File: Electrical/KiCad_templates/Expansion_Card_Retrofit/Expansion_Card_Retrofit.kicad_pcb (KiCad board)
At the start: 4 copper layers, 26 x 30 mm, 51 parts, among them J1 Conn 10P, P1 USB_C_Plug_USB2.0, Q1 DMG1012T, Q2 Q_PMOS_SGD, Q3 Q_Dual_NPN_NPN_C2E2C1E1B1B2, U1 AP2112K-3.3, U2 RP2040, U3 W25Q16JVUXIQ, U4 RP2040, U5 W25Q16JVUXIQ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

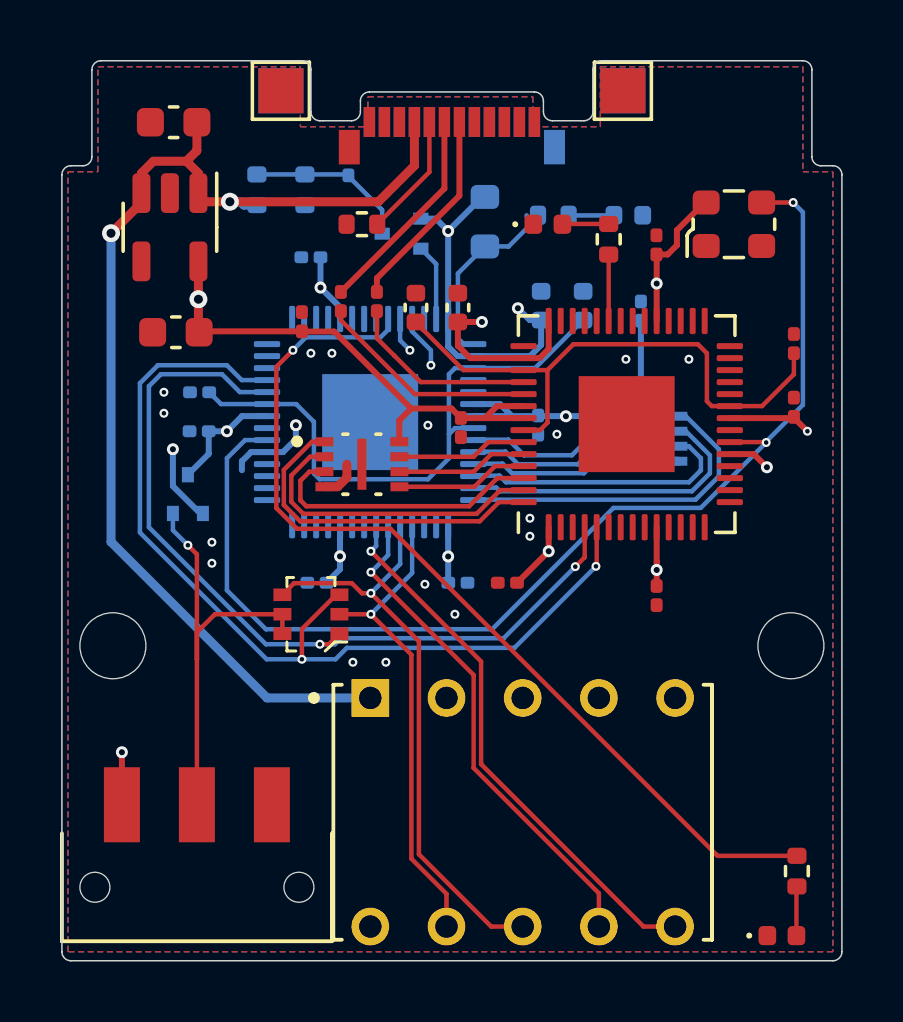
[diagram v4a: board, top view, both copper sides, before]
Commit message: All footprints placed single-sided
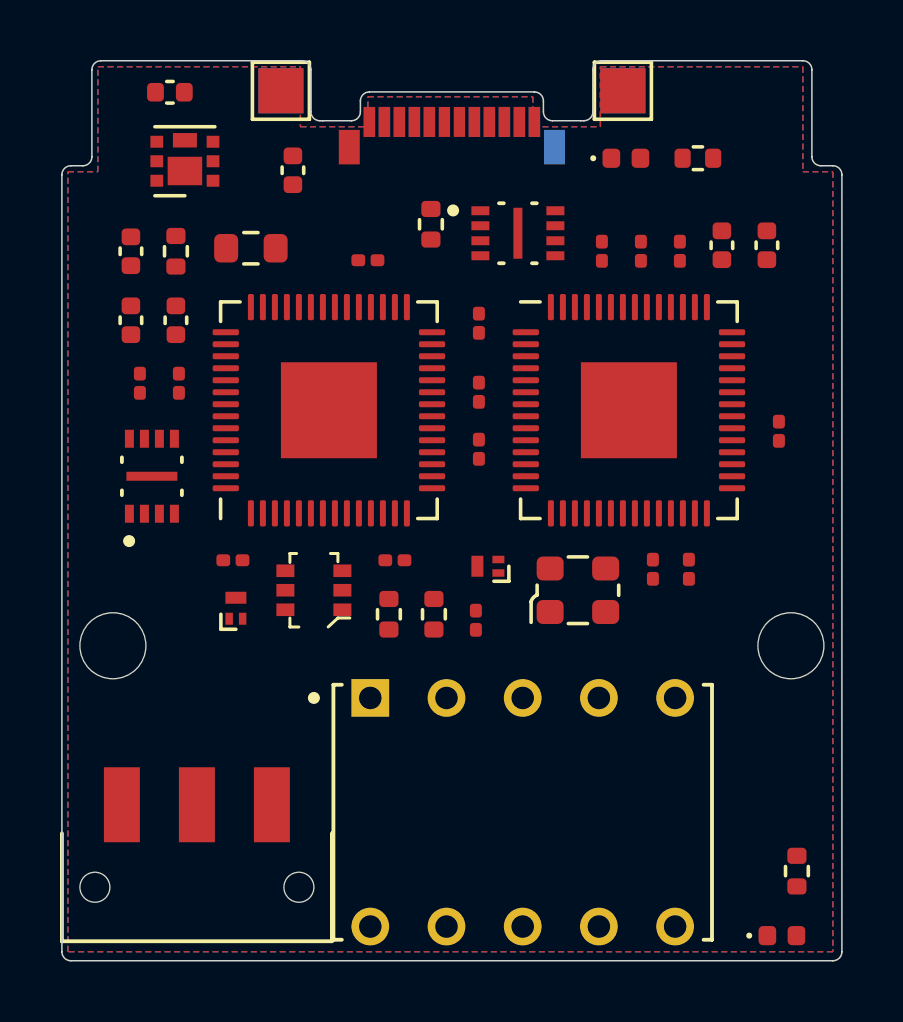
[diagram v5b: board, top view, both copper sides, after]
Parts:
- removed C17, C23: 100n, Capacitor_SMD:C_0201_0603Metric
- C1, C2: footprint Capacitor_SMD:C_0603_1608Metric -> Capacitor_SMD:C_0402_1005Metric
- C10, C11, C18, C22, C24, C5, C6, C7, C8, C9, R11, R12, R15, R16, U2, U3: moved to F.Cu
- Q1, Q2: footprint Package_TO_SOT_SMD:SOT-523 -> Package_DFN_QFN:Diodes_DFN1006-3; moved to F.Cu
- U1: value AP2112K-3.3 -> AP7366EA-3.3; footprint Package_TO_SOT_SMD:SOT-23-5 -> Package_DFN_QFN:Diodes_UDFN2020-6_Type-F
- moved C11 16.9 mm to (129.9, 95.8)
- moved C9 16.6 mm to (129.6, 91.4), turned to 90 degrees
- moved U3 16.3 mm to (130.3, 98.9), turned to 90 degrees
- moved C18 15.7 mm to (141.1, 103.7), turned to -90 degrees
- moved C7 15.1 mm to (129.6, 93.7)
- moved R15 14.8 mm to (138.2, 103.5)
- moved R16 14.8 mm to (139.7, 103.5)
- moved X1 13.3 mm to (144.5, 102.7)
- moved R12 12.6 mm to (131.1, 91.4), turned to -90 degrees
- moved C8 12.2 mm to (131.1, 93.7)
- moved C6 12.1 mm to (131.2, 95.8), turned to 90 degrees
- moved Q1 11.5 mm to (141.5, 101.9)
- moved C15 10.5 mm to (150.8, 91.2)
- moved C14 10.4 mm to (149.3, 91.2)
- moved R10 10.2 mm to (147.9, 91.4)
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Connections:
- C10 pad 1: /Development Board Section/3V3_DEV -> +3V3
- C11 pad 1: /Development Board Section/3V3_DEV -> +3V3
- C12 pad 1: +1V1 -> /Debug Probe Section/1V1_CORE
- C14 pad 1: +1V1 -> /Debug Probe Section/1V1_CORE
- C22 pad 1: /Development Board Section/3V3_DEV -> +3V3
- C24 pad 1: /Development Board Section/3V3_DEV -> +3V3
- C5 pad 1: +1V1 -> /Development Board Section/1V1_CORE
- C6 pad 1: /Development Board Section/3V3_DEV -> +3V3
- C7 pad 1: +1V1 -> /Development Board Section/1V1_CORE
- C8 pad 1: /Development Board Section/3V3_DEV -> +3V3
- Q1 pad 1: /Development Board Section/3V3_DEV -> +3V3
- Q2 pad 3: /Development Board Section/3V3_DEV -> /Development Board Section/RUN
- R11 pad 1: /Development Board Section/3V3_DEV -> +3V3
- U1 pad 4: unconnected-(U1-NC-Pad4) -> +3V3
- U1 pad 5: +3V3 -> unconnected-(U1-NC-Pad5)
- U2 pad 1: /Development Board Section/3V3_DEV -> +3V3
- U2 pad 10: /Development Board Section/3V3_DEV -> +3V3
- U2 pad 22: /Development Board Section/3V3_DEV -> +3V3
- U2 pad 23: +1V1 -> /Development Board Section/1V1_CORE
- U2 pad 26: unconnected-(U2-RUN-Pad26) -> /Development Board Section/RUN
- U2 pad 33: /Development Board Section/3V3_DEV -> +3V3
- U2 pad 42: /Development Board Section/3V3_DEV -> +3V3
- U2 pad 44: /Development Board Section/3V3_DEV -> +3V3
- U2 pad 45: +1V1 -> /Development Board Section/1V1_CORE
- U2 pad 48: /Development Board Section/3V3_DEV -> +3V3
- U2 pad 49: /Development Board Section/3V3_DEV -> +3V3
- U2 pad 50: +1V1 -> /Development Board Section/1V1_CORE
- U3 pad 8: /Development Board Section/3V3_DEV -> +3V3
- U4 pad 23: +1V1 -> /Debug Probe Section/1V1_CORE
- U4 pad 45: +1V1 -> /Debug Probe Section/1V1_CORE
- U4 pad 50: +1V1 -> /Debug Probe Section/1V1_CORE
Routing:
- net +3V3: track 39.7 -> 0.00 mm, vias 8 -> 0
- net +1V1: track 38.6 -> 0.00 mm
- net VBUS: track 38.2 -> 0.00 mm, vias 2 -> 0
- net OSC_OUT: track 38.0 -> 0.00 mm, vias 2 -> 0
- net SWDIO: track 31.9 -> 0.00 mm, vias 2 -> 0
- net LED_EN: track 31.5 -> 0.00 mm, vias 1 -> 0
- net /Development Board Section/3V3_DEV: track 31.4 -> 0.00 mm, vias 7 -> 0
- net SWCLK: track 28.2 -> 0.00 mm, vias 2 -> 0
- net GPIO3: track 19.7 -> 0.00 mm, vias 1 -> 0
- net GPIO5: track 18.3 -> 0.00 mm, vias 1 -> 0
- net GPIO4: track 16.8 -> 0.00 mm, vias 1 -> 0
- net GPIO_ADC0: track 16.4 -> 0.00 mm, vias 1 -> 0
- net GPIO2: track 16.0 -> 0.00 mm, vias 1 -> 0
- net DEV_ENABLE: track 14.7 -> 0.00 mm, vias 1 -> 0
- net GPIO_ADC1: track 14.3 -> 0.00 mm, vias 1 -> 0
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- added copper zone on In2.Cu, net +3V3
- removed copper zone on In2.Cu, net /Development Board Section/3V3_DEV

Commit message: Single layer basic layout finished
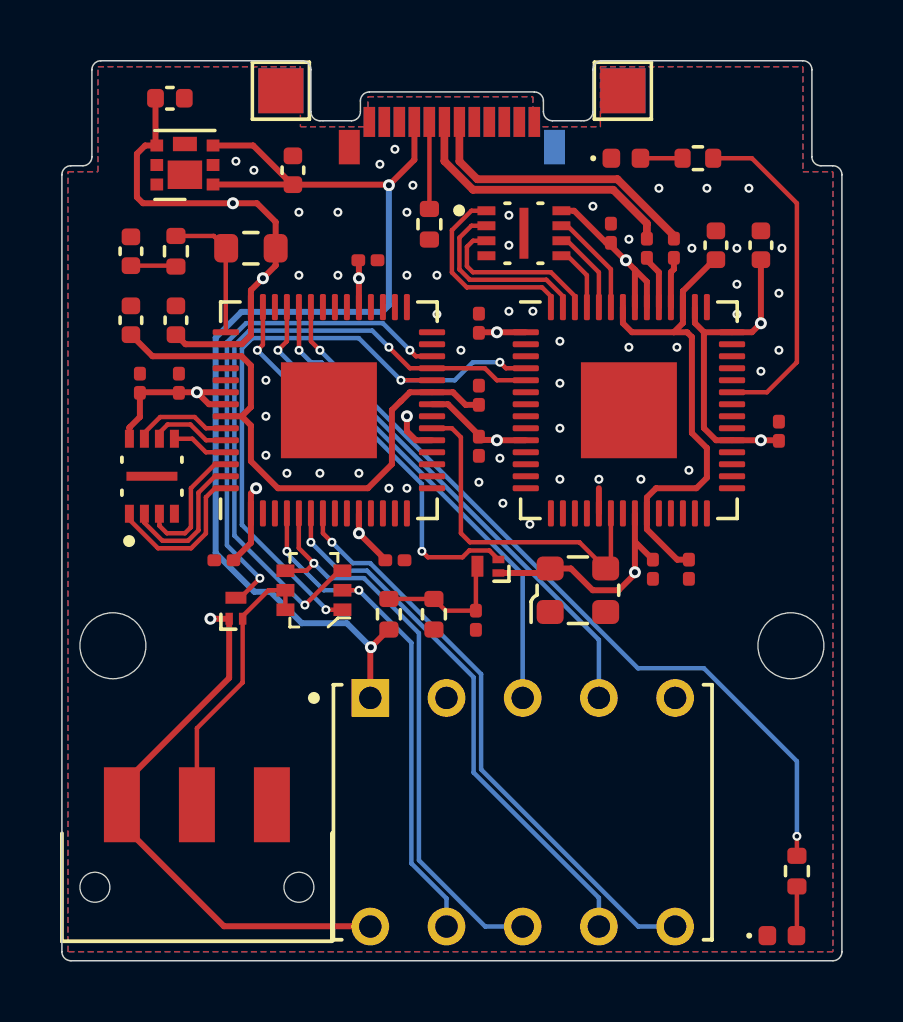
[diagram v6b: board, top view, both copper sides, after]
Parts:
- moved C13 0.67 mm to (145.6, 90.8)
- moved C10 0.30 mm to (132.7, 101.7)
- moved R10 0.22 mm to (147.7, 91.3)
- moved R9 0.22 mm to (146.8, 91.3)
- moved C14 0.20 mm to (149.1, 91.2)
- moved C15 0.20 mm to (150.6, 91.2)
- moved C2 0.20 mm to (130.9, 86.3)
- moved U5 0.20 mm to (142.7, 90.8)
- moved U1 0.12 mm to (131.4, 88.5)
- moved C5 0.10 mm to (141.2, 96.2), turned to 90 degrees
- moved C19 0.10 mm to (141.2, 97.9)
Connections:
- net USB_DN renamed USB_D_N
- net USB_DP renamed USB_D_P
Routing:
- net +3V3: track 0.00 -> 77.2 mm, vias 0 -> 13
- net VBUS: track 0.00 -> 38.0 mm, vias 0 -> 2
- net LED_EN: track 0.00 -> 26.3 mm, vias 0 -> 2
- net SWCLK: track 0.00 -> 22.0 mm, vias 0 -> 3
- net SWDIO: track 0.00 -> 22.0 mm, vias 0 -> 2
- net GPIO5: track 0.00 -> 19.7 mm, vias 0 -> 1
- net GPIO3: track 0.00 -> 19.3 mm, vias 0 -> 1
- net /Development Board Section/1V1_CORE: track 0.00 -> 18.9 mm
- net GPIO4: track 0.00 -> 18.3 mm, vias 0 -> 1
- net GPIO_ADC0: track 0.00 -> 17.4 mm, vias 0 -> 1
- net GPIO2: track 0.00 -> 17.2 mm, vias 0 -> 2
- net /Development Board Section/RUN: track 0.00 -> 16.9 mm, vias 0 -> 2
- net GPIO_ADC1: track 0.00 -> 16.9 mm, vias 0 -> 1
- net /Debug Probe Section/1V1_CORE: track 0.00 -> 16.1 mm
- net /Development Board Section/GPIO_ADC3: track 0.00 -> 13.9 mm, vias 0 -> 2
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- added copper zone on In1.Cu, net GND
- removed copper zone on In1.Cu, net +3V3

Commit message: Added edge pin connector
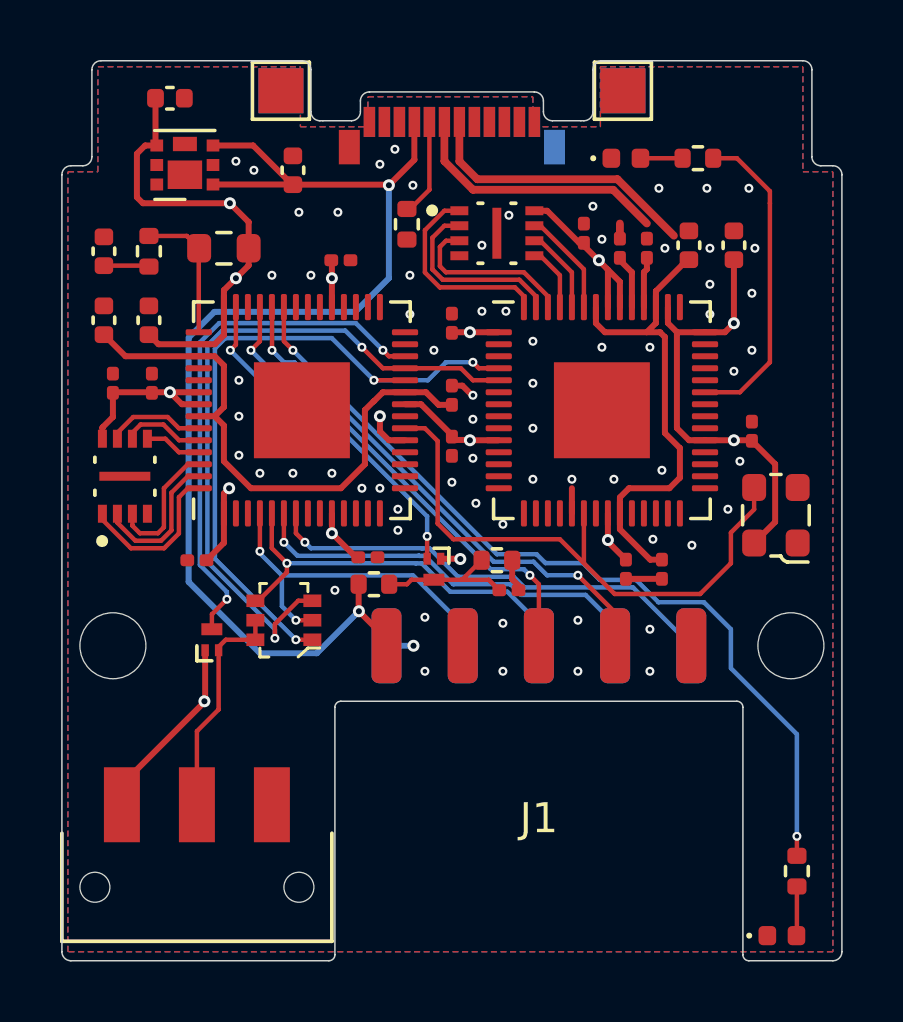
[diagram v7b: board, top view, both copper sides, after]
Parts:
- J1: footprint SnapEDA:AMPHENOL_89883-405LF -> SnapEDA:Pinheader_PCB_Edge_2x5_2.54mm
- moved X1 7.06 mm to (151.1, 100.2), turned to 180 degrees
- moved R16 2.77 mm to (141.8, 101.7), turned to 0 degrees
- moved Q1 1.80 mm to (139.7, 102.0), turned to -90 degrees
- moved C18 1.49 mm to (142.2, 102.7), turned to 0 degrees
- moved Q3 1.41 mm to (134.7, 103.7)
- moved Q2 1.32 mm to (132.3, 104.3)
- moved R15 1.12 mm to (137.7, 102.5), turned to 0 degrees
- moved C22 0.91 mm to (137.5, 101.6)
- moved C11 0.90 mm to (129.0, 95.8)
- moved C13 0.90 mm to (144.7, 90.8)
- moved C14 0.90 mm to (148.2, 91.2)
- moved C15 0.90 mm to (149.7, 91.2)
- moved C20 0.90 mm to (146.1, 102.0)
- moved C24 0.90 mm to (136.6, 91.7)
- moved C7 0.90 mm to (128.7, 93.7)
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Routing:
- net +3V3: track 77.2 -> 63.2 mm, vias 13 -> 15
- net OSC_OUT: track 11.5 -> 19.7 mm
- net GPIO3: track 19.3 -> 13.6 mm
- net GPIO2: track 17.2 -> 12.0 mm
- net GPIO4: track 18.3 -> 13.8 mm
- net GPIO5: track 19.7 -> 15.4 mm
- net GND: track 2.30 -> 5.42 mm, vias 53 -> 68
- net VBUS: track 38.0 -> 40.4 mm
- net LED_EN: track 26.3 -> 28.5 mm
- net /Development Board Section/GPIO_ADC3: track 13.9 -> 11.8 mm
- net DEV_ENABLE: track 9.35 -> 7.54 mm
- net SWDIO: track 22.0 -> 23.3 mm
- net SWCLK: track 22.0 -> 22.9 mm
- net /Development Board Section/RUN: track 16.9 -> 17.7 mm
- net /Debug Probe Section/LED_INT_EN: track 11.3 -> 10.6 mm
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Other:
- outline, holes or cut-outs redrawn

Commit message: Layout finished
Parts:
- S1: value JS102011SAQN -> Würth_450404015514; footprint SnapEDA:SW_JS102011SAQN -> SnapEDA:450404015514
- moved S1 0.61 mm to (131.9, 113.2), turned to 180 degrees
- moved J1 0.48 mm to (143.2, 111.3)
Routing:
- net DEV_ENABLE: track 7.54 -> 8.59 mm
- net GPIO2: track 12.0 -> 12.7 mm
- net GPIO5: track 15.4 -> 16.0 mm
- net +3V3: track 63.2 -> 63.7 mm
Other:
- outline, holes or cut-outs redrawn
